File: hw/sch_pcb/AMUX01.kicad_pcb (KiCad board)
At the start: 2 copper layers, 40.1 x 40.1 mm, 8 parts, among them J1 Umin ... Umax, M1 HOLE M3, M2 HOLE M3, M3 HOLE, M4 HOLE

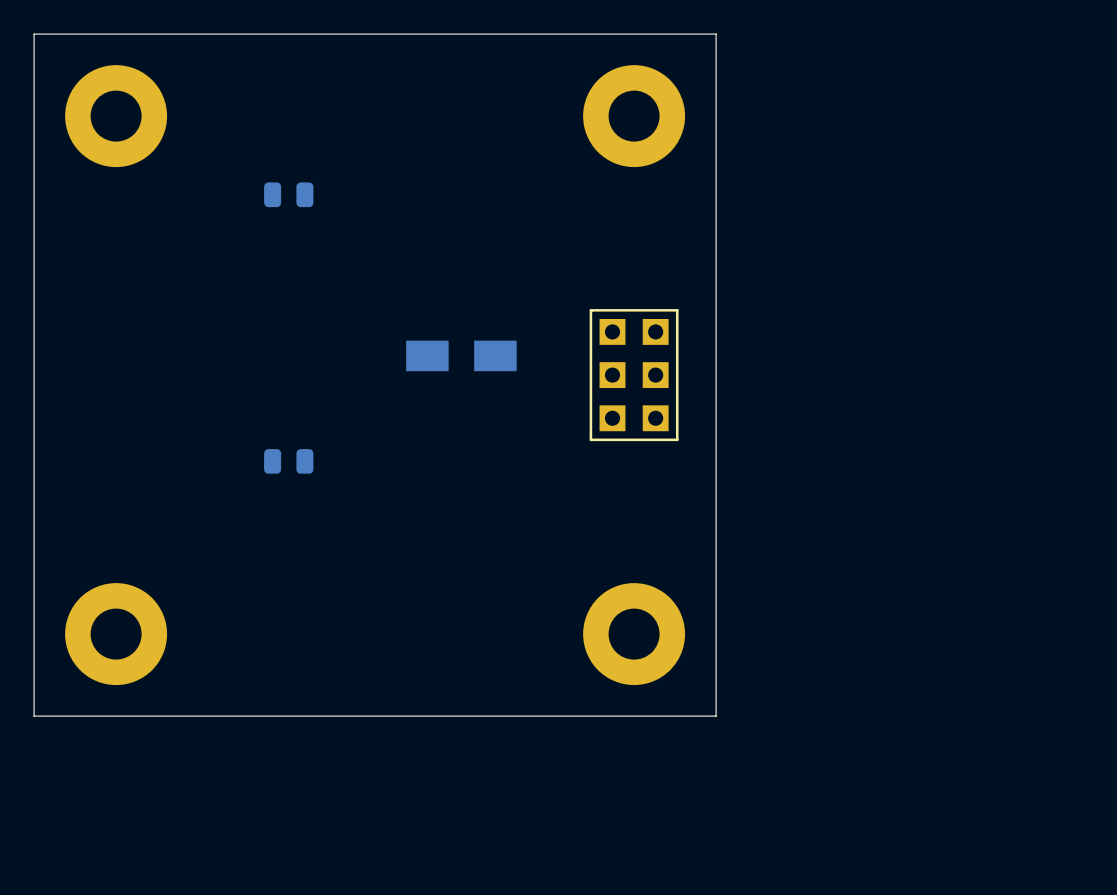
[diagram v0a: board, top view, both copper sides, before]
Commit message: Change address setup. Use script to make module layout. Update PCB from schematics.
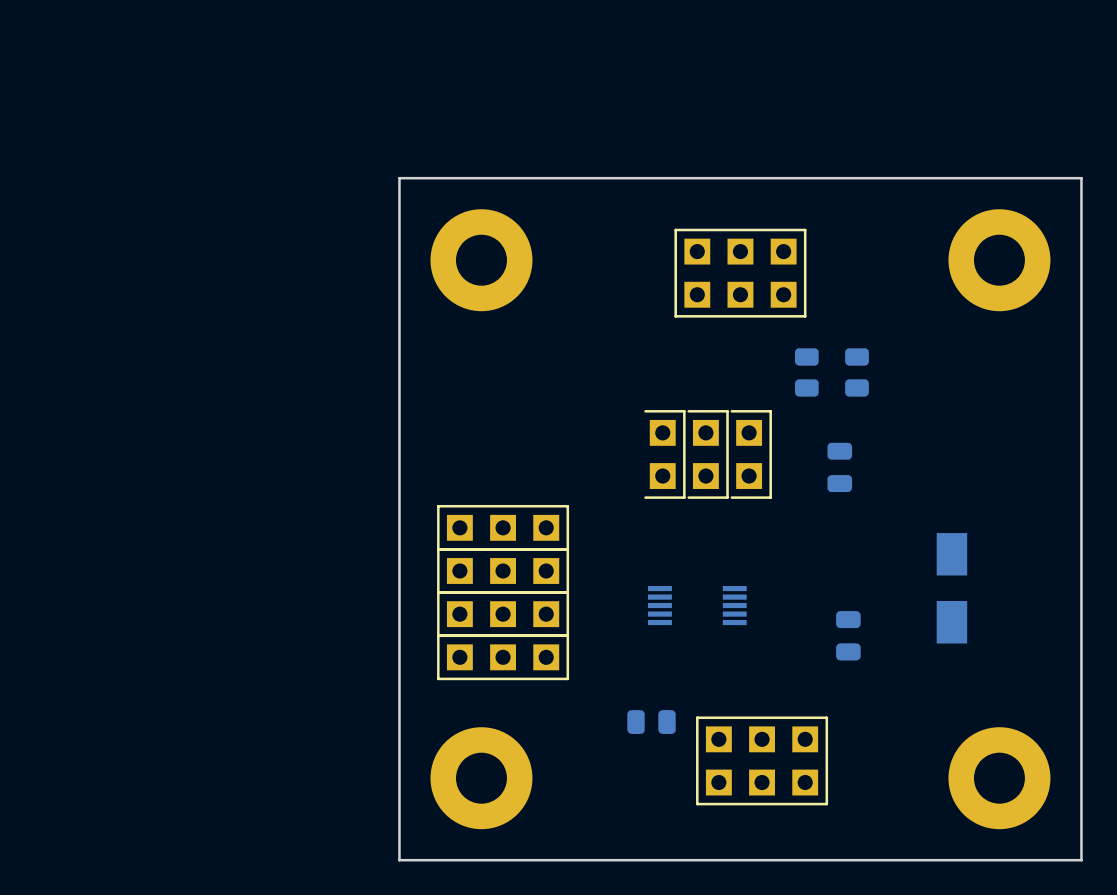
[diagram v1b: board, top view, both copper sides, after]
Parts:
- added J2: HEADER_1x03, Mlab_Pin_Headers:Straight_1x03, F.Cu at (134.5, 113.1)
- added J3: HEADER_1x03, Mlab_Pin_Headers:Straight_1x03, F.Cu at (134.5, 105.5)
- added J4: HEADER_1x03, Mlab_Pin_Headers:Straight_1x03, F.Cu at (134.5, 110.6)
- added J5: HEADER_1x03, Mlab_Pin_Headers:Straight_1x03, F.Cu at (134.5, 108.0)
- added J6: HEADER_2x03_PARALLEL, Mlab_Pin_Headers:Straight_2x03, F.Cu at (149.8, 119.2)
- added J7: HEADER_1x02, Mlab_Pin_Headers:Straight_2x01, F.Cu at (143.9, 101.2)
- added J8: HEADER_1x02, Mlab_Pin_Headers:Straight_2x01, F.Cu at (146.5, 101.2)
- added J9: HEADER_1x02, Mlab_Pin_Headers:Straight_2x01, F.Cu at (149.0, 101.2)
- added R1: 10k, Resistor_SMD:R_0805_2012Metric, B.Cu at (152.4, 96.4)
- added R2: 10k, Resistor_SMD:R_0805_2012Metric, B.Cu at (155.4, 96.4)
- added R3: 10k, Resistor_SMD:R_0805_2012Metric, B.Cu at (143.3, 116.9)
- added U1: MAX4734EUB+, Package_SO:MSOP-10_3x3mm_P0.5mm, B.Cu at (146.0, 110.1)
- J1: value Umin ... Umax -> 1.6 V to 3.6V
- moved M2 52.7 mm to (163.7, 89.8)
- moved C2 36.2 mm to (154.3, 102.0), turned to -90 degrees
- moved C1 34.5 mm to (154.8, 111.9), turned to -90 degrees
- moved D1 31.9 mm to (160.9, 109.1), turned to -90 degrees
- moved M4 23.1 mm to (163.7, 120.2)
- moved M3 23.1 mm to (133.3, 120.2)
- moved M1 12.4 mm to (133.3, 89.8)
- moved J1 8.67 mm to (148.5, 90.5), turned to -90 degrees
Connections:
- net +5V renamed +3V3
